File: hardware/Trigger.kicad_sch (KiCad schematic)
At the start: 11 parts, among them U6 MCP47FEB02A0T-E/ST, U7 Opamp_Dual

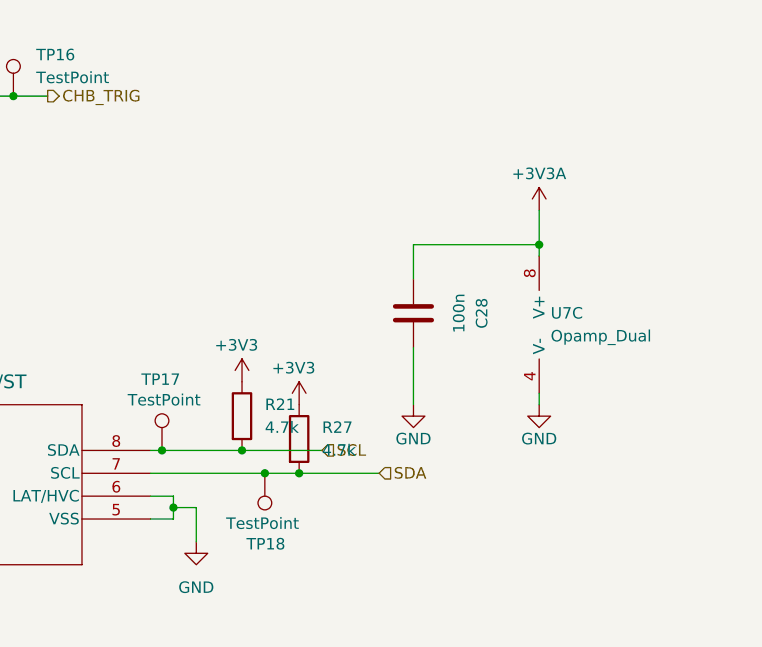
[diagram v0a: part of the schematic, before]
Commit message: fix(hardware): Fix swapped i2c pins
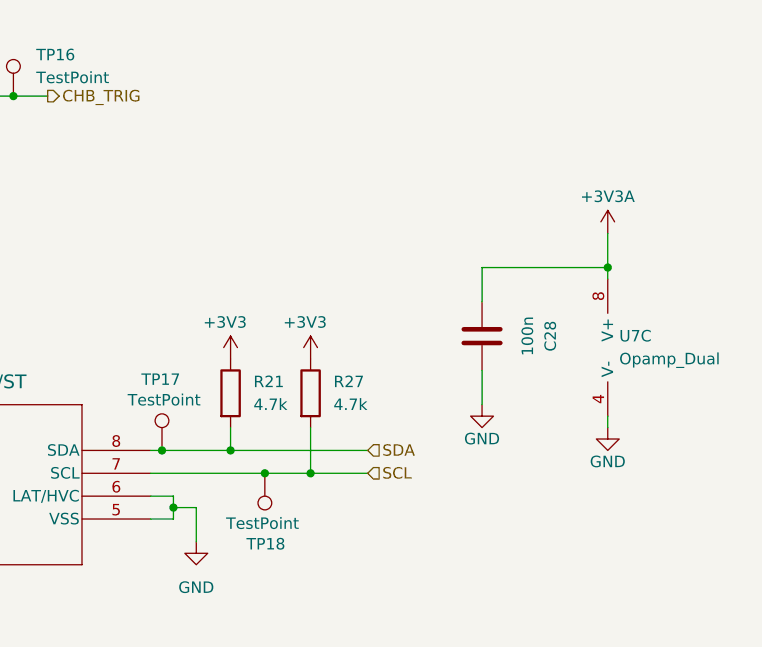
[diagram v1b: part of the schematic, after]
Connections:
- net SCL: now also R27.2, TP18.1, U6.7 (SCL); no longer R21.2, TP17.1, U6.8 (SDA)
- net SDA: now also R21.2, TP17.1, U6.8 (SDA); no longer R27.2, TP18.1, U6.7 (SCL)
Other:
- moved on the sheet: C28, R21, R27, U7C

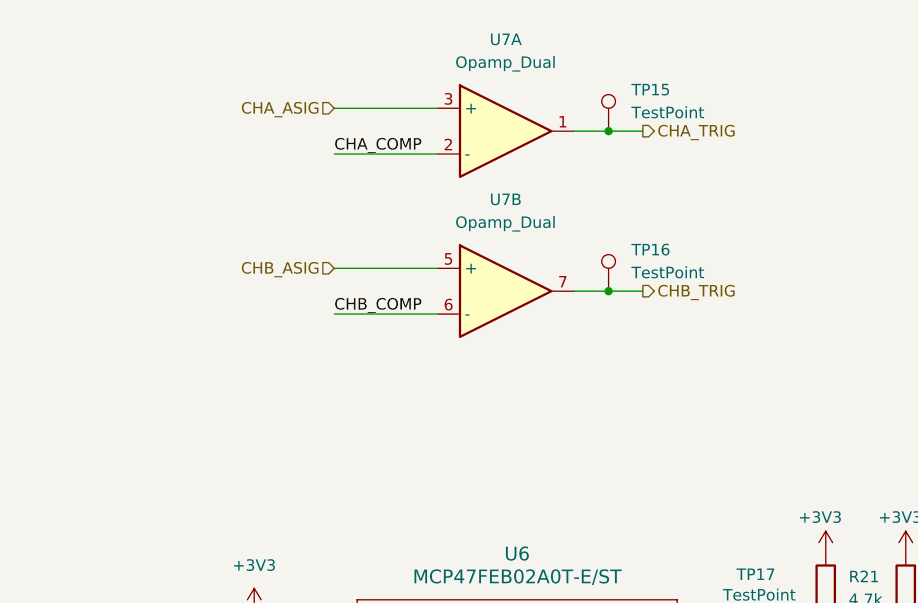
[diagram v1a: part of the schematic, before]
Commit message: feat(hardware): Add 30mV hysteresis to trigger
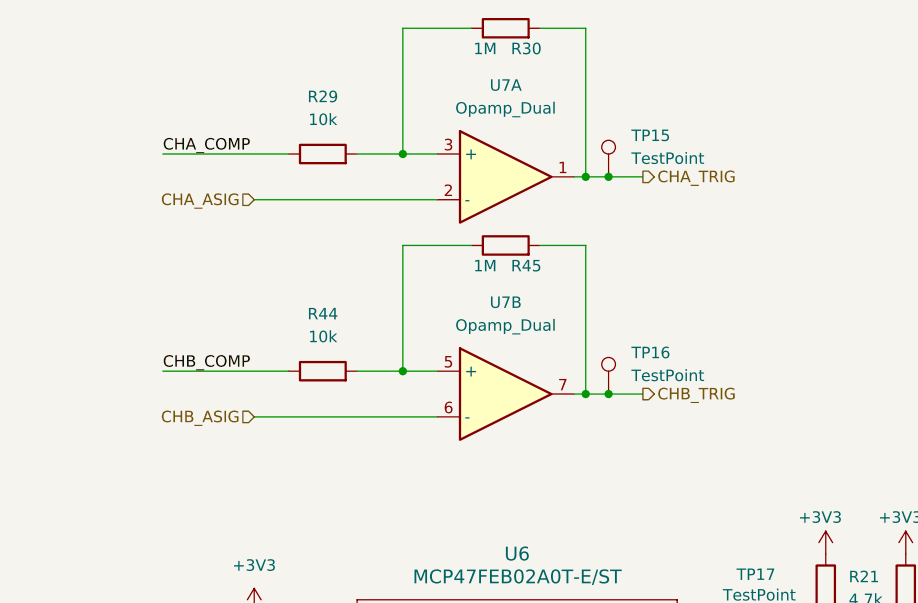
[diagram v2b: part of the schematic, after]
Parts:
- added R29, R44: 10k, symbol Device:R
- added R30, R45: 1M, symbol Device:R
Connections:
- net CHA_ASIG: now also U7.2 (-); no longer U7.3 (+)
- net CHA_COMP: now also R29.1; no longer U7.2 (-)
- net CHA_TRIG: now also R30.2
- net CHB_ASIG: now also U7.6 (-); no longer U7.5 (+)
- net CHB_COMP: now also R44.1; no longer U7.6 (-)
- net CHB_TRIG: now also R45.2
- new net: R44.2, R45.1, U7.5 (+)
- new net: R29.2, R30.1, U7.3 (+)
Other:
- moved on the sheet: TP15, TP16, U7A, U7B

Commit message: fix(hardware): Fix routing issues
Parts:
- R29, R30, R44, R45: footprint (none) -> Resistor_SMD:R_0402_1005Metric
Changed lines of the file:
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@@
 			)
 		)
-		(property "Footprint" ""
+		(property "Footprint" "Resistor_SMD:R_0402_1005Metric"
 			(at 85.09 41.148 90)
 			(effects
@@
 			)
 		)
-		(property "Footprint" ""
+		(property "Footprint" "Resistor_SMD:R_0402_1005Metric"
 			(at 64.77 55.118 90)
 			(effects
@@
 			)
 		)
-		(property "Footprint" ""
+		(property "Footprint" "Resistor_SMD:R_0402_1005Metric"
 			(at 64.77 30.988 90)
 			(effects
@@
 			)
 		)
-		(property "Footprint" ""
+		(property "Footprint" "Resistor_SMD:R_0402_1005Metric"
 			(at 85.09 17.018 90)
 			(effects
